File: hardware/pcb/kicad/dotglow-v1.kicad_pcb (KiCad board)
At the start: 2 copper layers, 128 x 33 mm, 40 parts, among them J1 USB-C 5V, J2 DISPLAY IN, J3 DHT22, J4 I2C (RTC V2), J5 SPEAKER 8R 2W, J6 LDR, SW1 RESET, SW2 BOOT, SW3 STOPWATCH, U1 ESP32-S3-MINI-1-N8, U2 AP2112K-3.3, U3 74AHCT125, U4 MAX98357A, U5 USBLC6-2SC6

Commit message: DotGlow V1 board: stopwatch header J7, routing rerun, layout-only package for EasyEDA (outline, DXF, placement CSV)
Co-Authored-By: ElectroIoT <electroiot.in@gmail.com>
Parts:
- added J7: STOPWATCH SW, Connector_PinHeader_2.54mm:PinHeader_1x02_P2.54mm_Vertical, F.Cu at (107.0, 77.0)
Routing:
- net GND: track 178.6 -> 0.00 mm, vias 153 -> 125
- net STOPWATCH: track 45.5 -> 50.8 mm
- net I2C_SCL: track 119.0 -> 122.0 mm
- net +5V: track 150.6 -> 148.9 mm, vias 22 -> 19
- net +3V3: track 174.8 -> 176.2 mm, vias 19 -> 16
- net DHT_DATA: track 99.7 -> 100.9 mm
- net LDR_ADC: vias 4 -> 3
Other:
- board text added: "SW"

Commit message: DotGlow V1 board: switch to ESP32-S3-WROOM-1-N16R8 (C2913202), full pinout doc, display header on the module end, rebuild script
Co-Authored-By: ElectroIoT <electroiot.in@gmail.com>
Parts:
- U1: value ESP32-S3-MINI-1-N8 -> ESP32-S3-WROOM-1-N16R8; footprint RF_Module:ESP32-S2-MINI-1 -> RF_Module:ESP32-S3-WROOM-1
- moved J5 4.00 mm to (120.0, 75.0)
- moved J7 4.00 mm to (111.0, 77.0)
- moved SW1 4.00 mm to (84.0, 77.0)
- moved SW2 4.00 mm to (94.0, 77.0)
- moved SW3 4.00 mm to (104.0, 77.0)
- moved TP1 4.00 mm to (127.0, 77.0)
- moved TP2 4.00 mm to (131.0, 77.0)
- moved J2 3.53 mm to (175.5, 61.4)
- moved R1 3.20 mm to (80.0, 64.5)
- moved C4 2.83 mm to (80.0, 69.0)
- moved U1 2.50 mm to (62.8, 66.5)
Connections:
- U1 pad 10: I2S_LRC -> unconnected-(U1-IO17-Pad10)
- U1 pad 11: I2S_DIN -> unconnected-(U1-IO18-Pad11)
- U1 pad 13: I2C_SCL -> USB_DN
- U1 pad 14: MAX_CS_3V -> USB_DP
- U1 pad 15: MAX_DIN_3V -> unconnected-(U1-IO3-Pad15)
- U1 pad 16: MAX_CLK_3V -> unconnected-(U1-IO46-Pad16)
- U1 pad 17: DHT_DATA -> I2C_SCL
- U1 pad 18: unconnected-(U1-IO14-Pad18) -> MAX_CS_3V
- U1 pad 19: AMP_SD -> MAX_DIN_3V
- U1 pad 2: GND -> +3V3
- U1 pad 20: unconnected-(U1-IO16-Pad20) -> MAX_CLK_3V
- U1 pad 21: unconnected-(U1-IO17-Pad21) -> DHT_DATA
- U1 pad 23: USB_DN -> unconnected-(U1-IO21-Pad23)
- U1 pad 24: USB_DP -> unconnected-(U1-IO47-Pad24)
- U1 pad 27: unconnected-(U1-IO47-Pad27) -> BOOT
- U1 pad 3: +3V3 -> EN
- U1 pad 38: unconnected-(U1-IO42-Pad38) -> NTC_ADC
- U1 pad 39: unconnected-(U1-TXD0-Pad39) -> LDR_ADC
- U1 pad 4: BOOT -> STOPWATCH
- U1 pad 40: unconnected-(U1-RXD0-Pad40) -> GND
- U1 pad 41: unconnected-(U1-IO45-Pad41) -> GND
- U1 pad 5: LDR_ADC -> I2S_BCLK
- U1 pad 6: NTC_ADC -> I2S_LRC
- U1 pad 7: unconnected-(U1-IO3-Pad7) -> I2S_DIN
- U1 pad 8: STOPWATCH -> AMP_SD
- U1 pad 9: I2S_BCLK -> unconnected-(U1-IO16-Pad9)
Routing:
- net +5V: track 148.9 -> 163.9 mm, vias 19 -> 16
- net NTC_ADC: track 107.0 -> 93.9 mm, vias 6 -> 2
- net MAX_CS_3V: track 79.7 -> 67.9 mm, vias 4 -> 0
- net MAX_DIN_3V: track 73.7 -> 62.1 mm, vias 4 -> 0
- net USB_DP: track 100.8 -> 89.8 mm, vias 2 -> 0
- net MAX_CLK_3V: track 81.7 -> 71.0 mm
- net I2C_SCL: track 122.0 -> 112.0 mm, vias 6 -> 3
- net AMP_SD: track 38.9 -> 48.7 mm
- net USB_DN: track 102.1 -> 93.5 mm, vias 2 -> 0
- net DHT_DATA: track 100.9 -> 93.2 mm
- net EN: track 48.9 -> 43.0 mm, vias 5 -> 4
- net STOPWATCH: track 50.8 -> 56.3 mm, vias 2 -> 7
- net I2C_SDA: track 120.9 -> 125.8 mm, vias 3 -> 6
- net +3V3: track 176.2 -> 171.5 mm, vias 16 -> 18
- net SPK_N: track 37.7 -> 42.0 mm, vias 1 -> 3
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
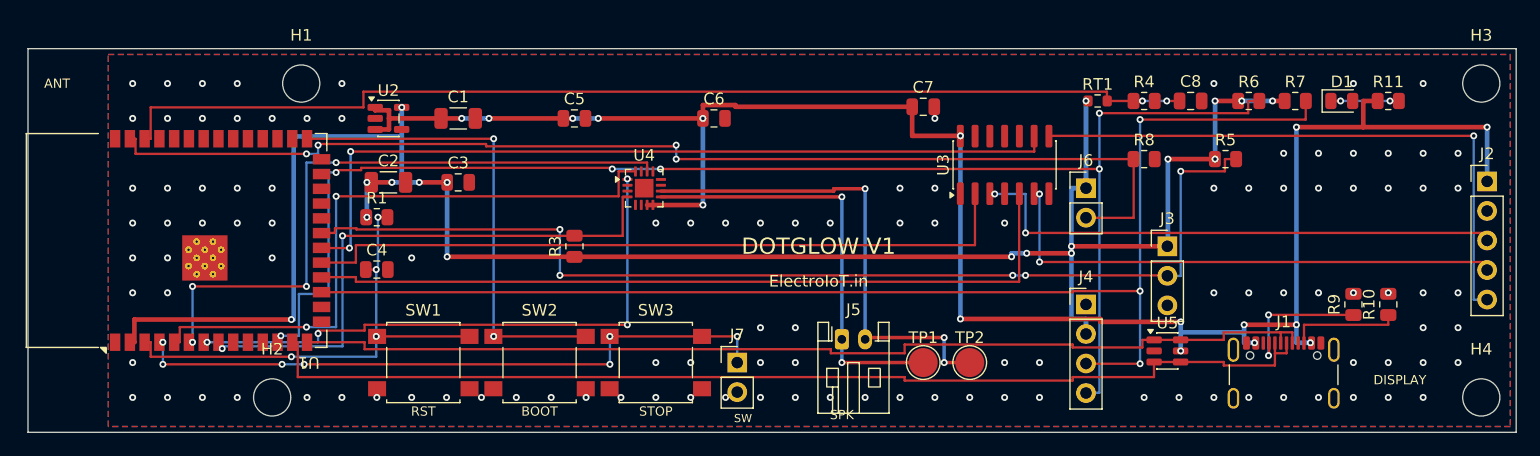
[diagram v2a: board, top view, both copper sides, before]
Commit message: DotGlow V1 board: JST XA connectors (2-pin C265077, 3-pin C265055, 4-pin C491709) for speaker, stopwatch, LDR, DHT22, I2C; re-placed and re-routed
Co-Authored-By: ElectroIoT <electroiot.in@gmail.com>
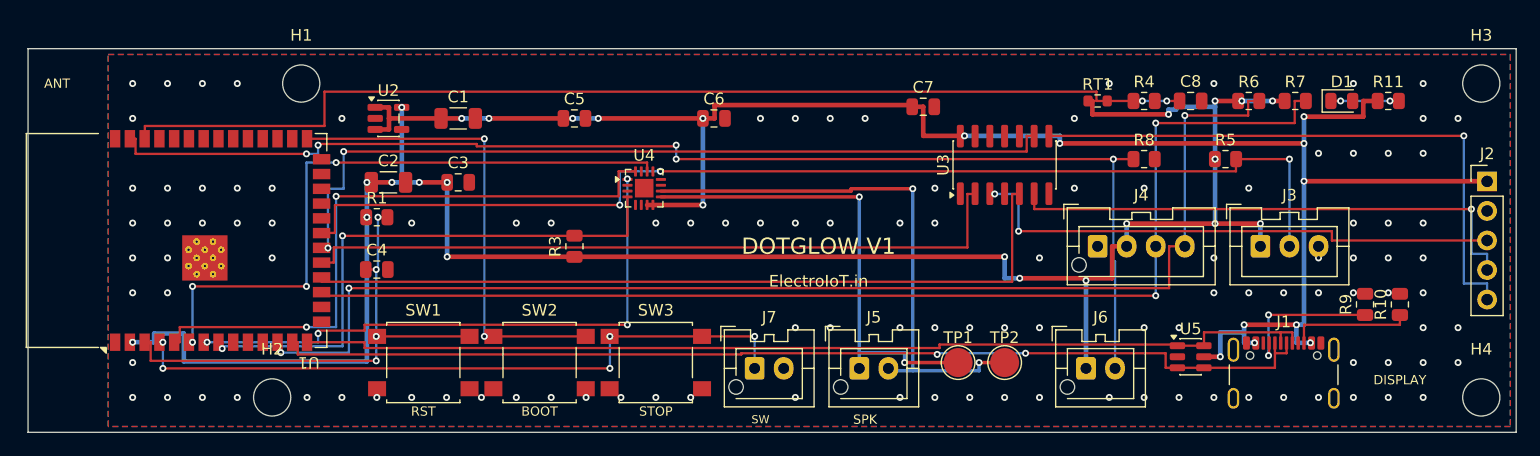
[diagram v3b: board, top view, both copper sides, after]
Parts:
- J3: footprint Connector_PinHeader_2.54mm:PinHeader_1x03_P2.54mm_Vertical -> Connector_JST:JST_XA_B03B-XASK-1_1x03_P2.50mm_Vertical
- J4: footprint Connector_PinHeader_2.54mm:PinHeader_1x04_P2.54mm_Vertical -> Connector_JST:JST_XA_B04B-XASK-1-A_1x04_P2.50mm_Vertical
- J5: footprint Connector_JST:JST_PH_S2B-PH-K_1x02_P2.00mm_Horizontal -> Connector_JST:JST_XA_B02B-XASK-1-A_1x02_P2.50mm_Vertical
- J6, J7: footprint Connector_PinHeader_2.54mm:PinHeader_1x02_P2.54mm_Vertical -> Connector_JST:JST_XA_B02B-XASK-1-A_1x02_P2.50mm_Vertical
- moved J6 15.5 mm to (141.0, 77.5)
- moved J3 8.00 mm to (156.0, 67.0)
- moved J4 5.10 mm to (142.0, 67.0)
- moved TP1 3.00 mm to (130.0, 77.0)
- moved TP2 3.00 mm to (134.0, 77.0)
- moved J5 2.92 mm to (121.5, 77.5)
- moved U5 2.06 mm to (150.0, 76.5)
- moved J7 1.58 mm to (112.5, 77.5)
- moved R10 1.00 mm to (168.0, 72.0)
- moved R9 1.00 mm to (165.0, 72.0)
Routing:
- net I2C_SDA: track 125.8 -> 107.0 mm, vias 6 -> 3
- net I2C_SCL: track 112.0 -> 101.7 mm, vias 3 -> 2
- net LDR_ADC: track 99.1 -> 108.2 mm, vias 4 -> 5
- net +5V: track 163.9 -> 157.2 mm
- net SPK_N: track 42.0 -> 48.4 mm, vias 3 -> 2
- net SPK_P: track 36.8 -> 41.1 mm
- net DHT_DATA: track 93.2 -> 97.1 mm, vias 5 -> 3
- net +3V3: track 171.5 -> 174.2 mm, vias 18 -> 19
- net STOPWATCH: track 56.3 -> 59.0 mm, vias 7 -> 5
- net USB_DN: track 93.5 -> 91.1 mm, vias 0 -> 2
- net USB_DP: track 89.8 -> 88.6 mm
- net CC2: track 9.65 -> 10.6 mm
- net CC1: track 12.0 -> 13.0 mm
- net EN: track 43.0 -> 43.7 mm
- net DISP_CS: vias 2 -> 1

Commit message: DotGlow V1 board: final EasyEDA files (schematic, PCB, BOM, Gerber), 3D renders and viewer angles, README banner, HyperFrames short video source
Co-Authored-By: ElectroIoT <electroiot.in@gmail.com>
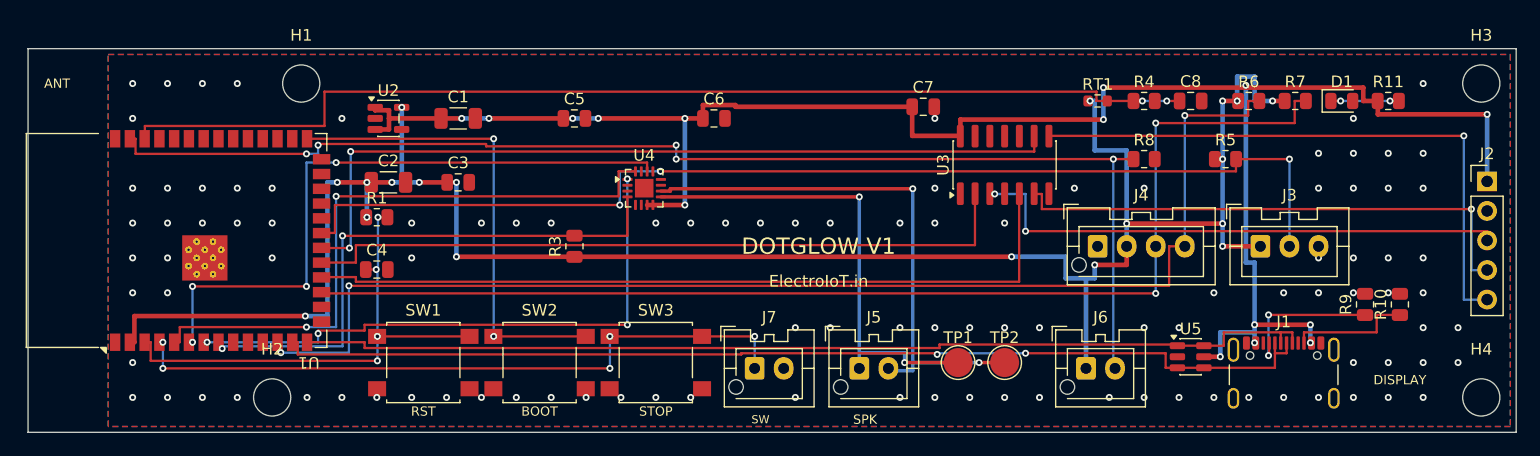
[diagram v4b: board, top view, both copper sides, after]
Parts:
- U2: value AP2112K-3.3 -> XC6220B331MR-G
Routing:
- net +5V: track 157.2 -> 161.6 mm, vias 16 -> 15
- net +3V3: track 174.2 -> 177.9 mm
- net SPK_N: track 48.4 -> 47.7 mm
- net GND: vias 115 -> 107
